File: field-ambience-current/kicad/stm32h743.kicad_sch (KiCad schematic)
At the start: 47 parts, among them J4 SWD 1.27mm (SWCLK/GND/SWDIO), U1 STM32H743VIT6 (480MHz M7, LQF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, Y1 8MHz ABLS-8.000MHZ-B4-T (CL=1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

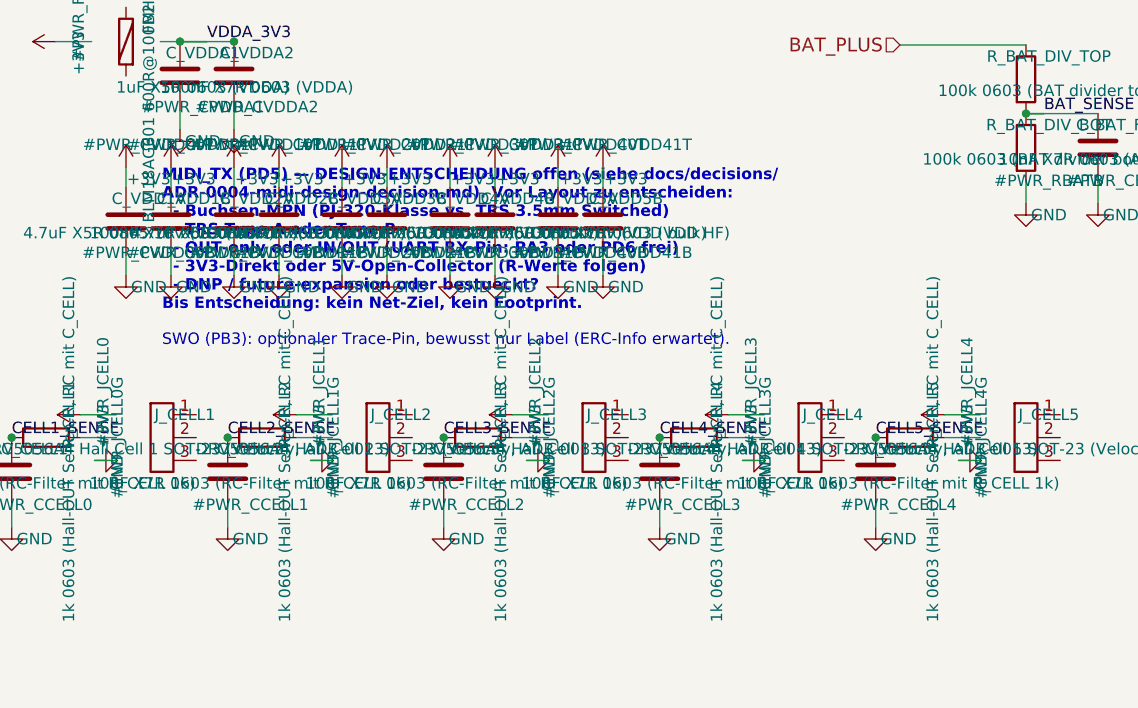
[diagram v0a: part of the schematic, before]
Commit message: feat(pcb): MIDI-Out (J10) — TRS Type A, 3.3V on PD5 (#68)
* docs(pcb): completeness package — pinmap, JLC BOM export, handoff doc

Make the PCB design data component- and connectivity-complete so a PCB
engineer knows every pin / net / module without re-deriving from the
generator. Closes the gaps from the hardware gap analysis: the BOM alone
isn't production-ready, the generator is the source of truth, and the
pinmap / machine BOM / handoff package were missing.

New deliverables:
- docs/hardware/PINMAP.md — every STM32H743 LQFP-100 pin (all 100) → net →
  function/AF → module → external-component pin, plus per-module net tables
  (source → all sinks) for Power/MCU/LCD/MCP+LEDs/Encoders/Audio/Battery,
  and the verified free-pin list. Distilled from the generator NETS table.
- kicad/export_jlc_bom.py — stdlib-only JLC BOM exporter; parses the 7
  generated leaf .kicad_sch, skips #PWR + DNP, groups by LCSC, quotes
  comma-bearing values. Parts without LCSC go to a stderr NO-LCSC list
  (no guessing). Prints that CPL needs a routed .kicad_pcb (doesn't exist).
- kicad/jlc_bom.csv — generated: 57 LCSC parts, 188 placements.
- docs/hardware/PCB_HANDOFF.md — what's in the package, the engineer
  workflow, and the hard blockers before a fab order (ERC in GUI, layout +
  routing, mechanical coords, Gerber/CPL — all KiCad-GUI / user-side since
  there is no kicad-cli in this env).

Generator: swap LED6/LED7 physical colors to spec — Shift = gelb (C2287),
Hold = gruen (C12624) — attribute-only (same footprint/pads/net), so the
schematic, BOM and firmware are now consistent. Regenerated mcp.kicad_sch.

Also: PROJECT_STATUS r18.64 (1.9" display freeze, per-world musical
identity, Echo/Blur); MECHANICAL_REQUIREMENTS 1.9" freeze line;
component_reviews/README F-1/F-2/F-3 status corrections.

Docs/kicad/tools only — outside the firmware CI path filter.

Co-Authored-By: Claude Opus 4.8 <noreply@anthropic.com>
Claude-Session: https://claude.ai/code/session_01K5kLTFpDCCoYwx2dq6RkAv

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
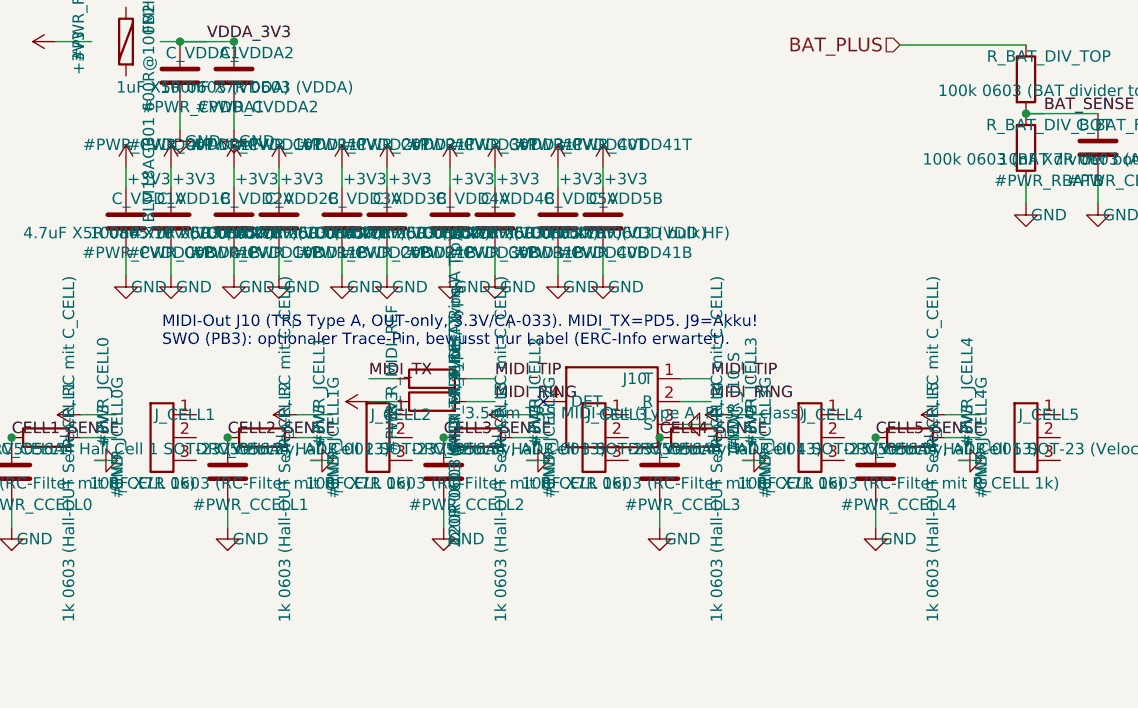
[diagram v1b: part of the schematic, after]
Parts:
- added J10: 3.5mm TRS MIDI-Out (Type A, PJ-320 class), field_ambience:Jack_3.5mm_PJ-320D_SMT, symbol Connector:AudioJack3_Switch
- added R_MIDI_REF: 220R 0603 (MIDI ref, Type-A Ring), Resistor_SMD:R_0603_1608Metric, symbol Device:R
- added R_MIDI_TX: 220R 0603 (MIDI TX series, Type-A Tip), Resistor_SMD:R_0603_1608Metric, symbol Device:R
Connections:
- net +3V3: now also R_MIDI_REF.1
- net GND: now also J10.3 (S)
- net MIDI_TX: now also R_MIDI_TX.1
- new net MIDI_RING: J10.2 (R), R_MIDI_REF.2
- new net MIDI_TIP: J10.1 (T), R_MIDI_TX.2
- no-connect marks 44 -> 45
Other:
- note added: "MIDI-Out J10 (TRS Type A, OUT-only, 3.3V/CA-033). MIDI_TX=PD5. J9=Akku!"
- note removed: "MIDI_TX (PD5) — DESIGN-ENTSCHEIDUNG offen (siehe docs/decisions/ ADR-0004-midi-design-decision.md). Vor Layout zu entscheiden: - Buchsen-MPN (PJ-320-Klasse vs. TRS 3.5mm Switched) - TRS Type A oder Type B - OUT-only oder IN/OUT (UART RX-Pin: PA3 oder PD6 frei) - 3V3-Direkt oder 5V-Open-Collector (R-Werte folgen) - DNP / future-expansion oder bestueckt? Bis Entscheidung: kein Net-Ziel, kein Footpr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"
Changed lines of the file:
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@@
       (project "field_ambience"
         (path "/e3bc855f-ca21-4bea-a5ff-d24a556f7f9e" (reference "#PWR_CCELL4") (unit 1)))))
+  (symbol (lib_id "Connector:AudioJack3_Switch") (at 150 258 0) (unit 1)
+    (in_bom yes) (on_board yes) (dnp no)
+      (property "Reference" "J10" (at 152.54 255.46 0)
+        (effects (font (size 1.27 1.27))))
+      (property "Value" "3.5mm TRS MIDI-Out (Type A, PJ-320 class)" (at 152.54 259.27 0)
+        (effects (font (size 1.27 1.27))))
+      (property "Footprint" "field_ambience:Jack_3.5mm_PJ-320D_SMT" (at 150 258 0)
+        (effects (font (size 1.27 1.27)) hide))
+      (property "Datasheet" "~" (at 150 258 0)
+        (effects (font (size 1.27 1.27)) hide))
+      (property "MPN" "PJ-320D (3.5mm TRS w/ switch)" (at 152.54 261.81 0)
+        (effects (font (size 1.27 1.27)) hide))
+      (property "LCSC" "C431535" (at 152.54 263.08 0)
+        (effects (font (size 1.27 1.27)) hide))
+    (instances
+      (project "field_ambience"
+        (path "/e3bc855f-ca21-4bea-a5ff-d24a556f7f9e" (reference "J10") (unit 1)))))
+  (symbol (lib_id "Power:GND") (at 161 260.54 270) (unit 1)
+    (in_bom yes) (on_board yes) (dnp no)
+      (property "Reference" "#PWR_J10_S" (at 163.54 258.0 0)
+        (effects (font (size 1.27 1.27))))
+      (property "Value" "GND" (at 163.54 261.81 0)
+        (effects (font (size 1.27 1.27))))
+      (property "Footprint" "" (at 161 260.54 0)
+        (effects (font (size 1.27 1.27)) hide))
+      (property "Datasheet" "~" (at 161 260.54 0)
+        (effects (font (size 1.27 1.27)) hide))
+    (instances
+      (project "field_ambience"
+        (path "/e3bc855f-ca21-4bea-a5ff-d24a556f7f9e" (reference "#PWR_J10_S") (unit 1)))))
+  (symbol (lib_id "Device:R") (at 130 255.46 90) (unit 1)
+    (in_bom yes) (on_board yes) (dnp no)
+      (property "Reference" "R_MIDI_TX" (at 132.54 252.92000000000002 0)
+        (effects (font (size 1.27 1.27))))
+      (property "Value" "220R 0603 (MIDI TX series, Type-A Tip)" (at 132.54 256.73 0)
+        (effects (font (size 1.27 1.27))))
+      (property "Footprint" "Resistor_SMD:R_0603_1608Metric" (at 130 255.46 0)
+        (effects (font (size 1.27 1.27)) hide))
+      (property "Datasheet" "~" (at 130 255.46 0)
+        (effects (font (size 1.27 1.27)) hide))
+      (property "MPN" "0603WAF2200T5E (220R 0603)" (at 132.54 259.27 0)
+        (effects (font (size 1.27 1.27)) hide))
+      (property "LCSC" "" (at 132.54 260.54 0)
+        (effects (font (size 1.27 1.27)) hide))
+    (instances
+      (project "field_ambience"
+        (path "/e3bc855f-ca21-4bea-a5ff-d24a556f7f9e" (reference "R_MIDI_TX") (unit 1)))))
+  (symbol (lib_id "Device:R") (at 130 258 90) (unit 1)
+    (in_bom yes) (on_board yes) (dnp no)
+      (property "Reference" "R_MIDI_REF" (at 132.54 255.46 0)
+        (effects (font (size 1.27 1.27))))
+      (property "Value" "220R 0603 (MIDI ref, Type-A Ring)" (at 132.54 259.27 0)
+        (effects (font (size 1.27 1.27))))
+      (property "Footprint" "Resistor_SMD:R_0603_1608Metric" (at 130 258 0)
+        (effects (font (size 1.27 1.27)) hide))
+      (property "Datasheet" "~" (at 130 258 0)
+        (effects (font (size 1.27 1.27)) hide))
+      (property "MPN" "0603WAF2200T5E (220R 0603)" (at 132.54 261.81 0)
+        (effects (font (size 1.27 1.27)) hide))
+      (property "LCSC" "" (at 132.54 263.08 0)
+        (effects (font (size 1.27 1.27)) hide))
+    (instances
+      (project "field_ambience"
+        (path "/e3bc855f-ca21-4bea-a5ff-d24a556f7f9e" (reference "R_MIDI_REF") (unit 1)))))
+  (symbol (lib_id "Power:+3V3") (at 123 258 90) (unit 1)
+    (in_bom yes) (on_board yes) (dnp no)
+      (property "Reference" "#PWR_R_MIDI_REF" (at 125.54 255.46 0)
+        (effects (font (size 1.27 1.27))))
+      (property "Value" "+3V3" (at 125.54 259.27 0)
+        (effects (font (size 1.27 1.27))))
+      (property "Footprint" "" (at 123 258 0)
+        (effects (font (size 1.27 1.27)) hide))
+      (property "Datasheet" "~" (at 123 258 0)
+        (effects (font (size 1.27 1.27)) hide))
+    (instances
+      (project "field_ambience"
+        (path "/e3bc855f-ca21-4bea-a5ff-d24a556f7f9e" (reference "#PWR_R_MIDI_REF") (unit 1)))))
   (wire (pts (xy 117.14 119.84) (xy 112.14 119.84))
     (stroke (width 0) (type default))
@@
     (stroke (width 0) (type default))
 )
+  (wire (pts (xy 157.62 255.46) (xy 161 255.46))
+    (stroke (width 0) (type default))
+)
+  (wire (pts (xy 157.62 258) (xy 161 258))
+    (stroke (width 0) (type default))
+)
+  (wire (pts (xy 157.62 260.54) (xy 161 260.54))
+    (stroke (width 0) (type default))
+)
+  (wire (pts (xy 126.19 255.46) (xy 123 255.46))
+    (stroke (width 0) (type default))
+)
+  (wire (pts (xy 133.81 255.46) (xy 137 255.46))
+    (stroke (width 0) (type default))
+)
+  (wire (pts (xy 126.19 258) (xy 123 258))
+    (stroke (width 0) (type default))
+)
+  (wire (pts (xy 133.81 258) (xy 137 258))
+    (stroke (width 0) (type default))
+)
   (junction (at 105.14 84.28) (diameter 0) (color 0 0 0 0)
 )
@@
     (effects (font (size 1.27 1.27)) (justify left bottom))
 )
+  (label "MIDI_TIP" (at 161 255.46 0) (fields_autoplaced)
+    (effects (font (size 1.27 1.27)) (justify left bottom))
+)
+  (label "MIDI_RING" (at 161 258 0) (fields_autoplaced)
+    (effects (font (size 1.27 1.27)) (justify left bottom))
+)
+  (label "MIDI_TX" (at 123 255.46 0) (fields_autoplaced)
+    (effects (font (size 1.27 1.27)) (justify left bottom))
+)
+  (label "MIDI_TIP" (at 137 255.46 0) (fields_autoplaced)
+    (effects (font (size 1.27 1.27)) (justify left bottom))
+)
+  (label "MIDI_RING" (at 137 258 0) (fields_autoplaced)
+    (effects (font (size 1.27 1.27)) (justify left bottom))
+)
   (hierarchical_label "DISPLAY_SW" (shape output) (at 104.14 119.84 0)
     (effects (font (size 1.524 1.524)) (justify right))
@@
     (effects (font (size 1.524 1.524)) (justify right))
 )
+  (no_connect (at 142.38 258)
+)
   (no_connect (at 117.14 117.3)
 )
@@
   (no_connect (at 142.54 201.12)
 )
-  (text "MIDI_TX (PD5) — DESIGN-ENTSCHEIDUNG offen (siehe docs/decisions/\nADR-0004-midi-design-decision.md). Vor Layout zu entscheiden:\n  - Buchsen-MPN (PJ-320-Klasse vs. TRS 3.5mm Switched)\n  - TRS Type A oder Type B\n  - OUT-only oder IN/OUT (UART RX-Pin: PA3 oder PD6 frei)\n  - 3V3-Direkt oder 5V-Open-Collector (R-Werte folgen)\n  - DNP / future-expansion oder bestueckt?\nBis Entscheidung: kein Net-Ziel, kein Footprint." (at 100 248 0)
-    (effects (font (size 1.27 1.27) bold) (justify left bottom))
+  (text "MIDI-Out J10 (TRS Type A, OUT-only, 3.3V/CA-033). MIDI_TX=PD5. J9=Akku!" (at 100 250 0)
+    (effects (font (size 1.27 1.27)) (justify left bottom))
 )
   (text "SWO (PB3): optionaler Trace-Pin, bewusst nur Label (ERC-Info erwartet)." (at 100 252 0)

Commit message: parts: resolve ECO items — MIDI LCSC, button SMD→THT, TPS22918 LCSC, pinmap (#79)
* docs(pcb): completeness package — pinmap, JLC BOM export, handoff doc

Make the PCB design data component- and connectivity-complete so a PCB
engineer knows every pin / net / module without re-deriving from the
generator. Closes the gaps from the hardware gap analysis: the BOM alone
isn't production-ready, the generator is the source of truth, and the
pinmap / machine BOM / handoff package were missing.

New deliverables:
- docs/hardware/PINMAP.md — every STM32H743 LQFP-100 pin (all 100) → net →
  function/AF → module → external-component pin, plus per-module net tables
  (source → all sinks) for Power/MCU/LCD/MCP+LEDs/Encoders/Audio/Battery,
  and the verified free-pin list. Distilled from the generator NETS table.
- kicad/export_jlc_bom.py — stdlib-only JLC BOM exporter; parses the 7
  generated leaf .kicad_sch, skips #PWR + DNP, groups by LCSC, quotes
  comma-bearing values. Parts without LCSC go to a stderr NO-LCSC list
  (no guessing). Prints that CPL needs a routed .kicad_pcb (doesn't exist).
- kicad/jlc_bom.csv — generated: 57 LCSC parts, 188 placements.
- docs/hardware/PCB_HANDOFF.md — what's in the package, the engineer
  workflow, and the hard blockers before a fab order (ERC in GUI, layout +
  routing, mechanical coords, Gerber/CPL — all KiCad-GUI / user-side since
  there is no kicad-cli in this env).

Generator: swap LED6/LED7 physical colors to spec — Shift = gelb (C2287),
Hold = gruen (C12624) — attribute-only (same footprint/pads/net), so the
schematic, BOM and firmware are now consistent. Regenerated mcp.kicad_sch.

Also: PROJECT_STATUS r18.64 (1.9" display freeze, per-world musical
identity, Echo/Blur); MECHANICAL_REQUIREMENTS 1.9" freeze line;
component_reviews/README F-1/F-2/F-3 status corrections.

Docs/kicad/tools only — outside the firmware CI path filter.

Co-Authored-By: Claude Opus 4.8 <noreply@anthropic.com>
Claude-Session: https://claude.ai/code/session_01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
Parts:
- R_MIDI_REF, R_MIDI_TX: LCSC (none) -> C22962
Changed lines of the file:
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@@
       (property "MPN" "0603WAF2200T5E (220R 0603)" (at 132.54 259.27 0)
         (effects (font (size 1.27 1.27)) hide))
-      (property "LCSC" "" (at 132.54 260.54 0)
+      (property "LCSC" "C22962" (at 132.54 260.54 0)
         (effects (font (size 1.27 1.27)) hide))
     (instances
@@
       (property "MPN" "0603WAF2200T5E (220R 0603)" (at 132.54 261.81 0)
         (effects (font (size 1.27 1.27)) hide))
-      (property "LCSC" "" (at 132.54 263.08 0)
+      (property "LCSC" "C22962" (at 132.54 263.08 0)
         (effects (font (size 1.27 1.27)) hide))
     (instances

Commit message: kicad(gen): flow the 5 sourcing-fix part swaps into the generator (r18.71)
The generator is the schematic's source of truth, so the BOM part swaps must
live here (previously only in BOM/HTML). Swapped LCSC + MPN in the generator,
regenerated the .kicad_sch, re-exported jlc_bom.csv:
- FB2 ferrite C84094 -> C19330 (same Murata MPN, JLC 950k)
- VCAP C24539 -> C23630 (2.2uF 16V X5R 0603, JLC Basic)
- charger LED C72041 (blue+EOL!) -> C965800 (orange 605nm 0603)
- C_BULK2 C2880380 (stock 1) -> C23742 (100uF 10V X5R 1210)
- modifier buttons SW6-10 C2845240 (stock 30) -> C36498965 (HX B3F square
  head); footprint SW_TC1212-7.3_THT_4P reused, HX pinout verify noted in FP_NOTE.

The generated schematic Aron opens now carries the correct in-stock parts.
check_pinmap passes; jlc_bom.csv has the new codes (old ones gone).

Co-Authored-By: Claude Opus 4.8 <noreply@anthropic.com>
Claude-Session: https://claude.ai/code/session_01K5kLTFpDCCoYwx2dq6RkAv
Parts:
- C_VCAP1, C_VCAP2: LCSC C24539 -> C23630; MPN CL10A225KP8NNNC -> CL10A225KO8NNNC; VERIFY-STOCK JLC Extended 2.2uF/10V X5R 0603 — falls out-of-stock altern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 -> (none)
- FB2: LCSC C84094 -> C19330
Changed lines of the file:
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@@
       (property "MPN" "BLM18AG601SN1D" (at 98.54 221.81 0)
         (effects (font (size 1.27 1.27)) hide))
-      (property "LCSC" "C84094" (at 98.54 223.08 0)
+      (property "LCSC" "C19330" (at 98.54 223.08 0)
         (effects (font (size 1.27 1.27)) hide))
     (instances
@@
       (property "Datasheet" "~" (at 112.14 83.01 0)
         (effects (font (size 1.27 1.27)) hide))
-      (property "MPN" "CL10A225KP8NNNC" (at 114.68 86.82000000000001 0)
+      (property "MPN" "CL10A225KO8NNNC" (at 114.68 86.82000000000001 0)
         (effects (font (size 1.27 1.27)) hide))
       (property "Manufacturer" "Samsung" (at 114.68 88.09 0)
         (effects (font (size 1.27 1.27)) hide))
-      (property "LCSC" "C24539" (at 114.68 89.36 0)
-        (effects (font (size 1.27 1.27)) hide))
-      (property "VERIFY-STOCK" "JLC Extended 2.2uF/10V X5R 0603 — falls out-of-stock alternative LCSC-Nr. waehlen" (at 114.68 90.63000000000001 0)
+      (property "LCSC" "C23630" (at 114.68 89.36 0)
         (effects (font (size 1.27 1.27)) hide))
     (instances
@@
       (property "Datasheet" "~" (at 112.14 85.55 0)
         (effects (font (size 1.27 1.27)) hide))
-      (property "MPN" "CL10A225KP8NNNC" (at 114.68 89.36 0)
+      (property "MPN" "CL10A225KO8NNNC" (at 114.68 89.36 0)
         (effects (font (size 1.27 1.27)) hide))
       (property "Manufacturer" "Samsung" (at 114.68 90.63 0)
         (effects (font (size 1.27 1.27)) hide))
-      (property "LCSC" "C24539" (at 114.68 91.89999999999999 0)
-        (effects (font (size 1.27 1.27)) hide))
-      (property "VERIFY-STOCK" "JLC Extended 2.2uF/10V X5R 0603 — falls out-of-stock alternative LCSC-Nr. waehlen" (at 114.68 93.17 0)
+      (property "LCSC" "C23630" (at 114.68 91.89999999999999 0)
         (effects (font (size 1.27 1.27)) hide))
     (instances

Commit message: cells: Hall/ADC → digital I²C switches on MCP23017 (ADR-0013 superseded, r18.73) (#85)
Per user direction (HiChord Batch 4+ reference): the 5 cells change from
Gateron-magnetic + DRV5056A4 Hall (analog velocity at the STM32 ADC) to plain
digital on/off tactile switches on the existing MCP23017 I²C expander — the
HiChord Batch 4+ topology (switch → I²C GPIO-expander → MCU).

No new component: SW1–SW5 reuse the same already-verified HX B3F-4055-Y
(LCSC C36498965) part as the modifier buttons SW6–SW10, on the already-free
expander pins GPA0–GPA4 (nets CELL1..5_BTN). This restores the original
SPEC v0.6 §7 "10 switches" topology (5 cells + 5 modifiers on the expander).

Generator (generate_kicad_project.py):
- mcp_sheet: NC_GPA0..4 placeholders → SW1–SW5 cell switches on GPA0–GPA4,
  mirroring the SW6–SW10 modifier wiring (pin → GND, MCP pull-up, shared INT).
- stm32 sheet: removed 5× DRV5056A4 (J_CELL1–5), 5× R_CELL 1k, 5× C_CELL 10nF;
  freed the 5 ADC pins PC0/PC1/PA4/PB0/PB1 as NC reserves (Rev-B option).
- Regenerated schematics, jlc_bom.csv (56 LCSC parts; DRV5056A4 gone, SW1–SW10
  all C36498965), and Aron's bom_overview.html.

Docs updated to match: BOM_MASTER §7, PCB_BOM, PINMAP, KICAD_BLUEPRINT,
SCHEMATIC_WALKTHROUGH, MECHANICAL_REQUIREMENTS, PCB_FOOTPRINT_RISK_AUDIT,
field_ambience_pcb_SPEC_v0.7 §5.6a, ADR-0013 (SUPERSEDED banner), ADR-0016
(Hall-current premise amended), mechanical_coordinates, PROJECT_QUALITY,
PROJECT_STATUS, CHANGELOG, COST_ESTIMATE. Hall kept as the documented option
only if expressive press-depth/velocity is wanted later.

Host tests green (352298 checks, 0 failures); firmware untouched.


Claude-Session: https://claude.ai/code/session_019pKguH6aG4iazMCWJnpmMn

Co-authored-by: Claude <noreply@anthropic.com>
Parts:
- removed C_CELL1, C_CELL2, C_CELL3, C_CELL4, C_CELL5: 10nF X7R 0603 (RC-Filter mit R_CELL 1k), Capacitor_SMD:C_0603_1608Metric, symbol Device:C
- removed J_CELL1: DRV5056A4 Hall Cell 1 SOT-23 (Velocity, ADR-0013), Package_TO_SOT_SMD:SOT-23, symbol Connector:Conn_01x03
- removed J_CELL2: DRV5056A4 Hall Cell 2 SOT-23 (Velocity, ADR-0013), Package_TO_SOT_SMD:SOT-23, symbol Connector:Conn_01x03
- removed J_CELL3: DRV5056A4 Hall Cell 3 SOT-23 (Velocity, ADR-0013), Package_TO_SOT_SMD:SOT-23, symbol Connector:Conn_01x03
- removed J_CELL4: DRV5056A4 Hall Cell 4 SOT-23 (Velocity, ADR-0013), Package_TO_SOT_SMD:SOT-23, symbol Connector:Conn_01x03
- removed J_CELL5: DRV5056A4 Hall Cell 5 SOT-23 (Velocity, ADR-0013), Package_TO_SOT_SMD:SOT-23, symbol Connector:Conn_01x03
- removed R_CELL1, R_CELL2, R_CELL3, R_CELL4, R_CELL5: 1k 0603 (Hall-OUT Serien-R, RC mit C_CELL), Resistor_SMD:R_0603_1608Metric, symbol Device:R
